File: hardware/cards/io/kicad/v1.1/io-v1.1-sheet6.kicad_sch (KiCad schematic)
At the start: 2 parts, among them IC8 74*06

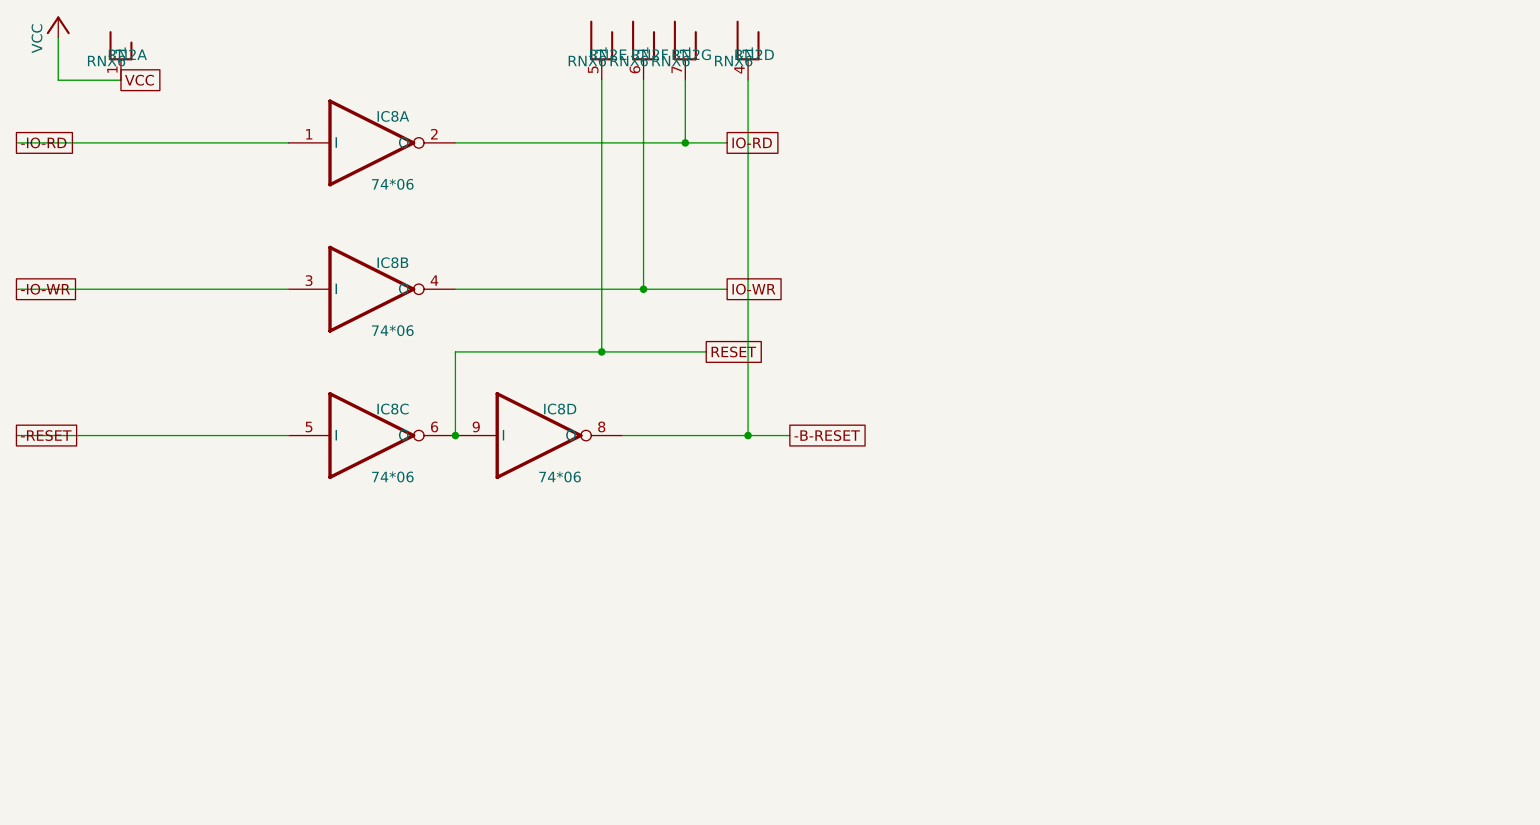
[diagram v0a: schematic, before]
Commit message: fix(kicad): readable converted schematics - overlaps 42,847 -> 3,147, nothing off the frame; CF sheet 0 overlaps
- tools/kicad/sch_overlaps.py: calibrated readability check (text/text, text/body, text/line, off frame/title block)
- eagle_sch_to_kicad.py: fields placed from Eagle's smashed attributes or the symbol's >NAME/>VALUE with Eagle's align,
  size and ratio, readable angles; fields Eagle never shows hidden (FABC96R shows only its pin name); pin numbers hidden
  where every Eagle pin hides them; Eagle-hidden layers dropped (the stray SpiceOrder text); labels on their own wires,
  converter labels only where KiCad needs them; rotate-then-mirror fixed for MR90/MR270 in pin_world/no-connects;
  each sheet on the smallest page that holds it, centred clear of the title block
- finish_board.py: stable footprint-library choice (DRC counts no longer vary run to run)
- all 37 projects regenerated: netlist proofs unchanged (34 MATCH, 2 schematic-only, video Fusion export MISMATCH as
  before); DRC same or better; ERC up (loose wire ends onto graphic buses no longer hidden by labels; explained per README)
- CF card: gate names off the gate bodies, U3 clear of its title, 5.08 mm connector pins; rebuilt: DRC 0/0, proof MATCH
- schematic PDFs regenerated (tools/sch_to_pdf.py, 37/37)

Co-Authored-By: Claude Opus 5.5 <noreply@anthropic.com>
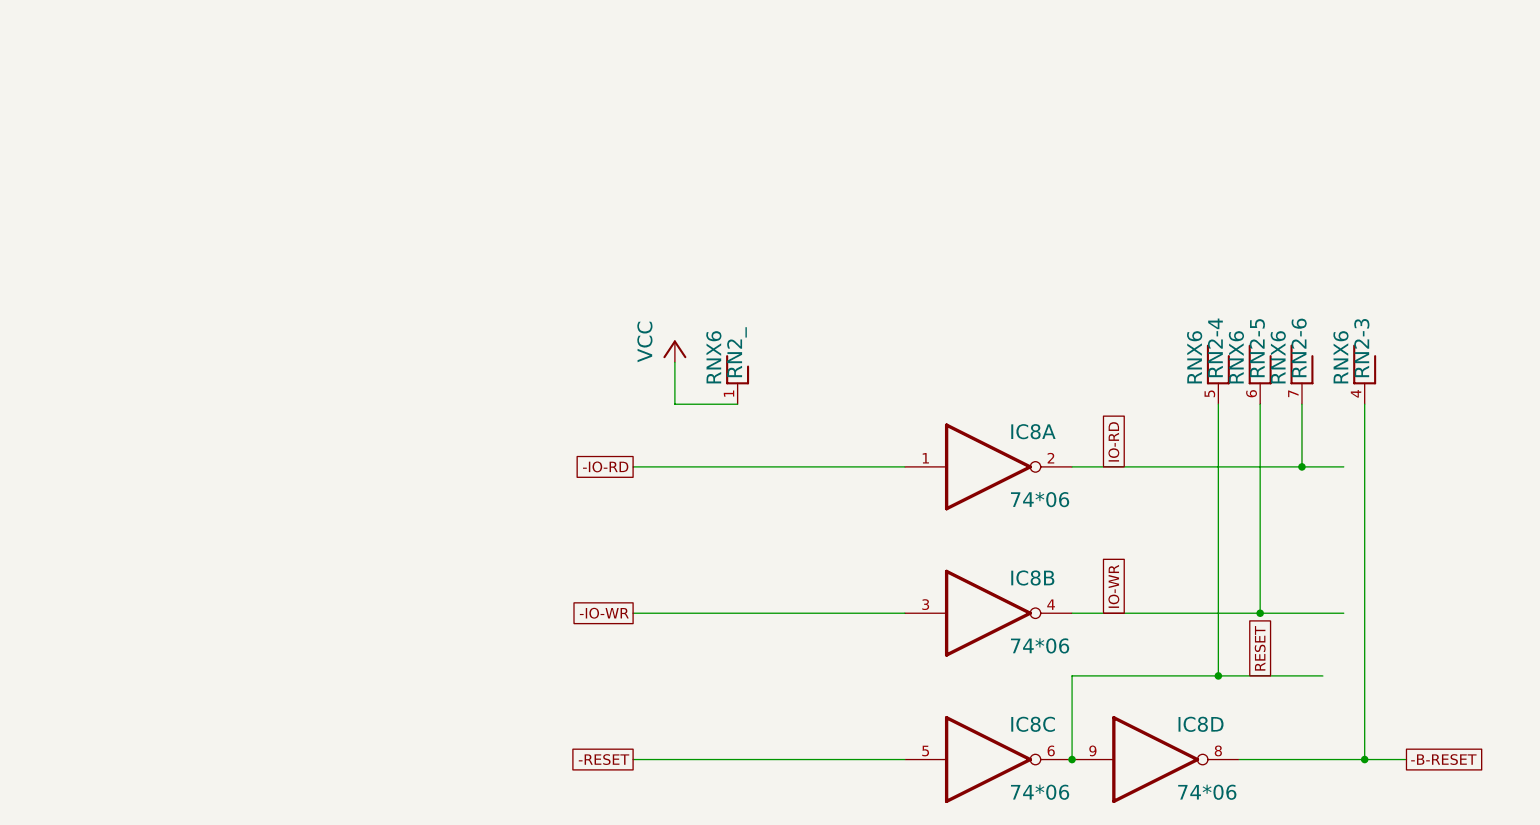
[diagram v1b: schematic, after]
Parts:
- RN2: Eagle name (none) -> RN2-6
- RN2: Eagle name (none) -> RN2-3
- RN2: Eagle name (none) -> RN2_
- RN2: Eagle name (none) -> RN2-5
- RN2: Eagle name (none) -> RN2-4
